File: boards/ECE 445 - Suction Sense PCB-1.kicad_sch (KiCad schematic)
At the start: 39 parts, among them J1 Paddle Sensor, J2 Motion Sensor, J3 Battery Connector, J4 Barrel_Jack, U1 ESP32-WROOM-32E, U2 TPS2121RUXR, U3 AP62150Z6, U4 MCP73831-2-OT

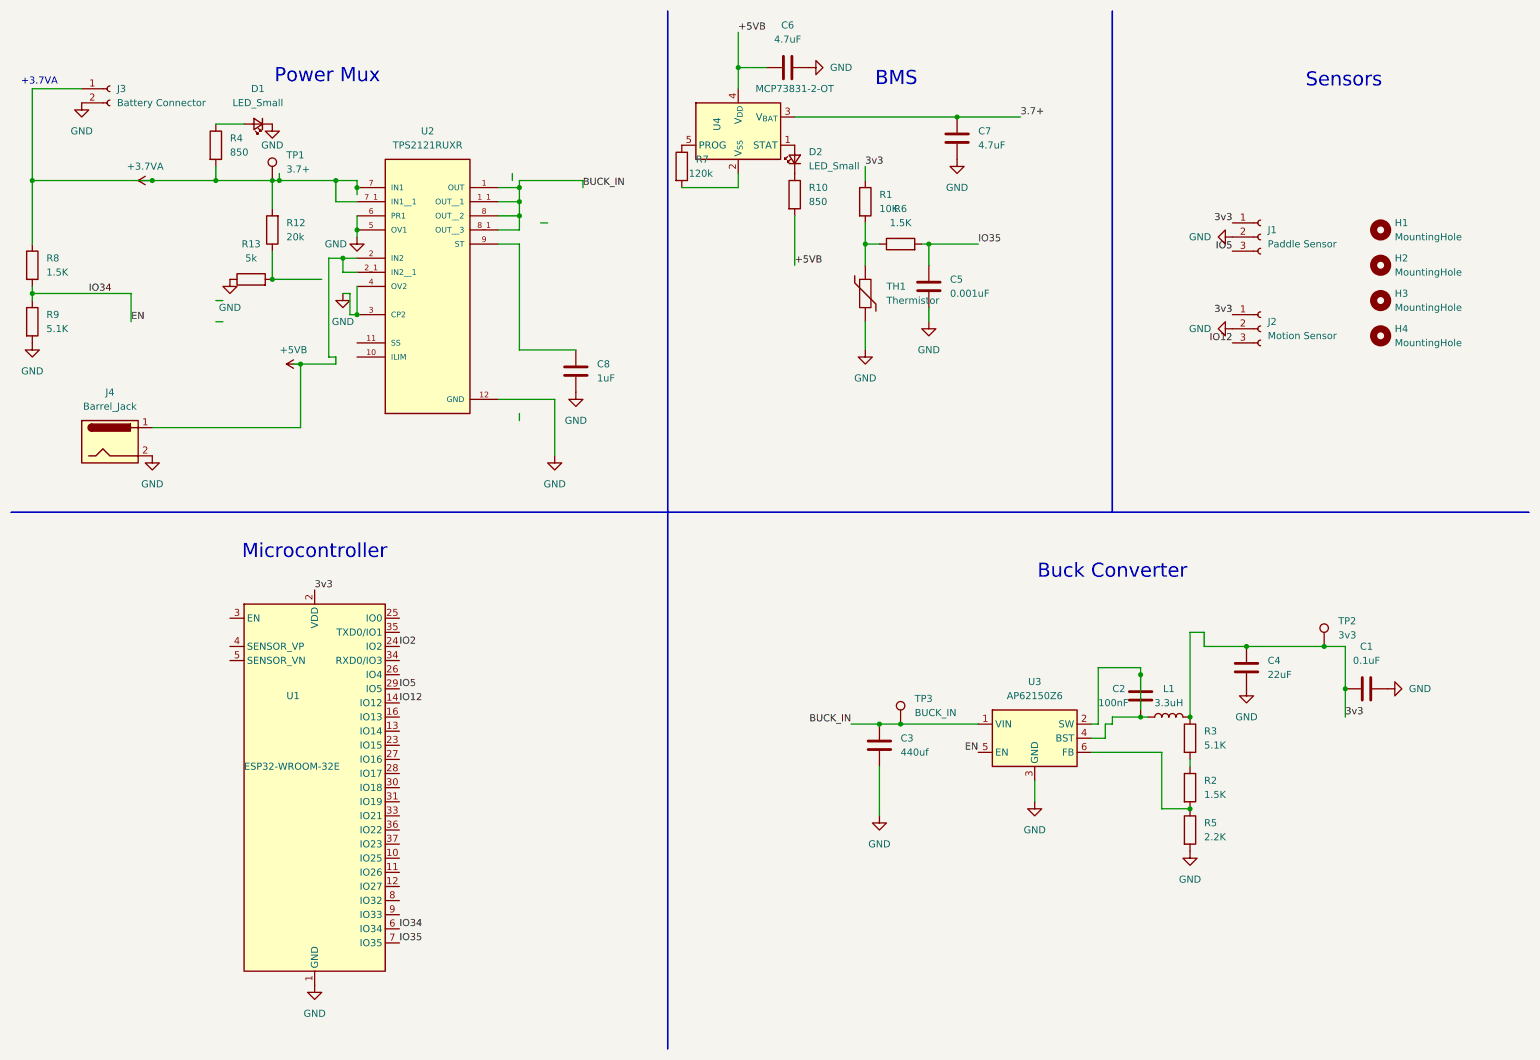
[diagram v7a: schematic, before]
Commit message: added boost converter
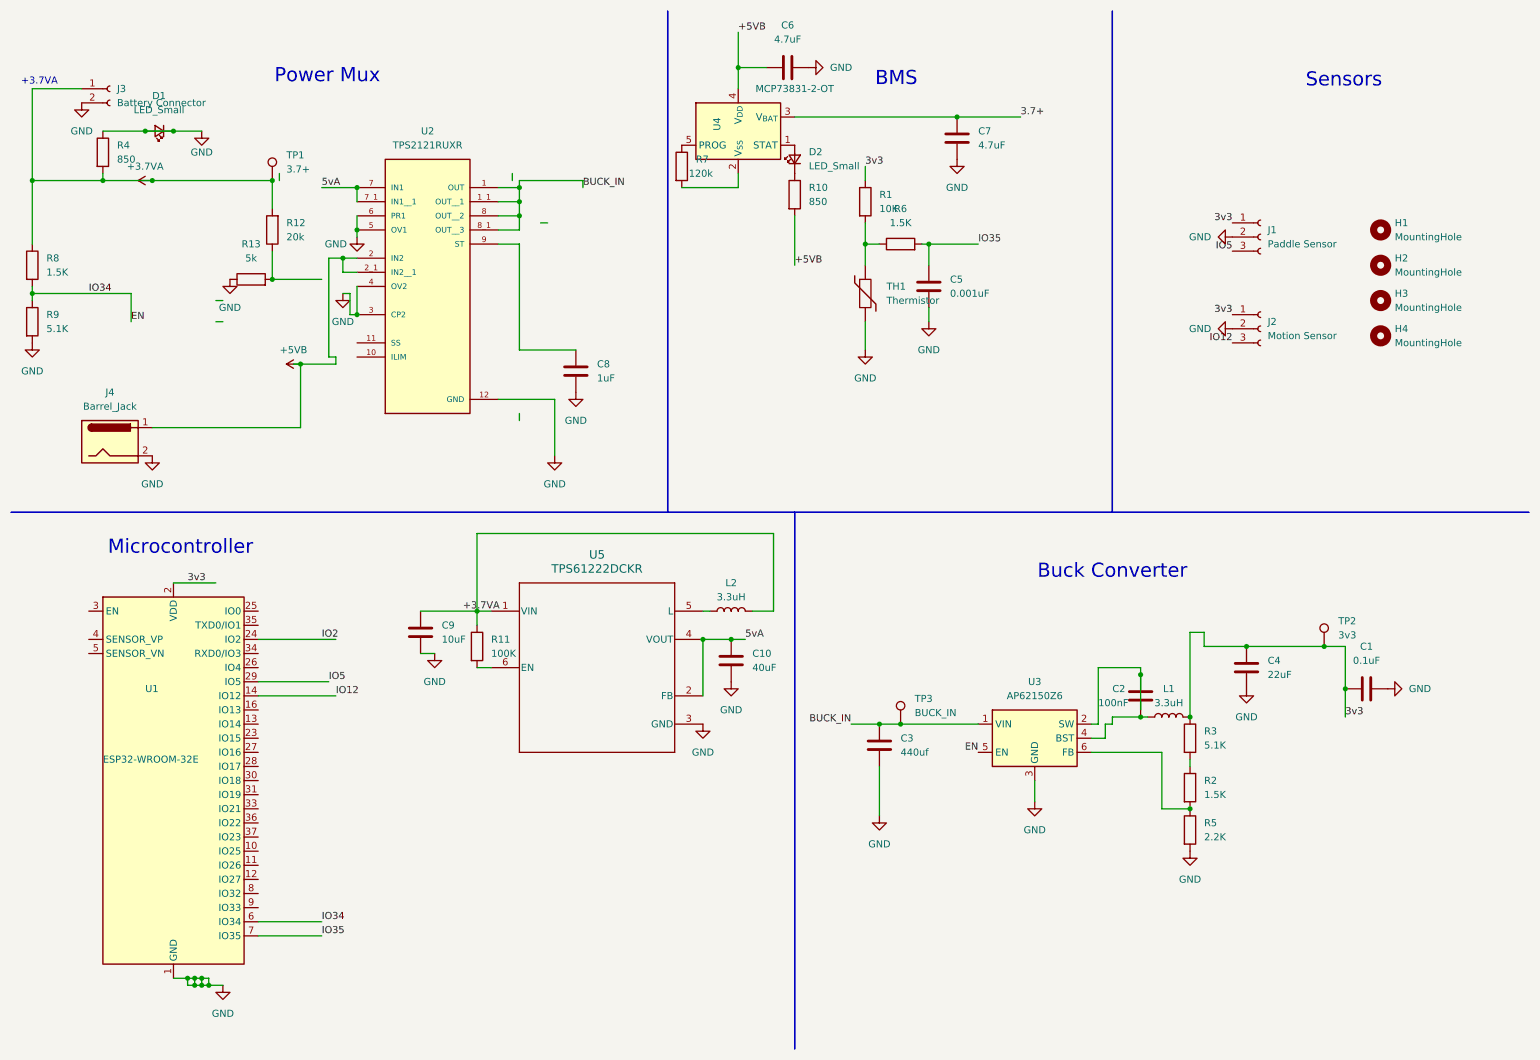
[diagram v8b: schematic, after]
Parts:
- added C10: 40uF, Capacitor_SMD:C_0805_2012Metric_Pad1.18x1.45mm_HandSolder, symbol Device:C
- added C9: 10uF, Capacitor_SMD:C_0805_2012Metric_Pad1.18x1.45mm_HandSolder, symbol Device:C
- added L2: 3.3uH, Inductor_SMD:L_0805_2012Metric_Pad1.15x1.40mm_HandSolder, symbol Device:L
- added R11: 100K, Resistor_SMD:R_0805_2012Metric_Pad1.20x1.40mm_HandSolder, symbol Device:R
- added U5: TPS61222DCKR, KiCadExtras:DCK0006A, symbol 2025-10-12_01-10-01:TPS61222DCKR
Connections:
- net +3.7VA: now also C9.1, L2.2, R11.1, U5.1 (VIN); no longer U2.7 (IN1), U2.7_1 (IN1__1)
- net GND: now also D1.2 (A), R4.1, C10.2, C9.2, U5.3 (GND)
- new net: L2.1, U5.5 (L)
- new net: R11.2, U5.6 (EN)
- new net 5vA: C10.1, U2.7 (IN1), U2.7_1 (IN1__1), U5.2 (FB), U5.4 (VOUT)
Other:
- moved on the sheet: D1, R4, U1
